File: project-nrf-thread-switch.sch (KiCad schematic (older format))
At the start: 14 parts, among them J1 Left, J2 Right

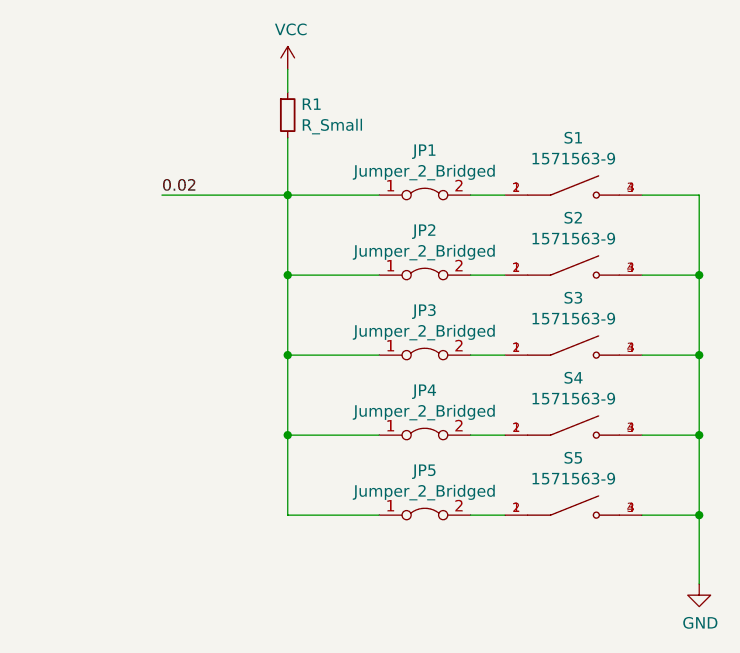
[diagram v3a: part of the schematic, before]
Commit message: Single button with header footprint fix
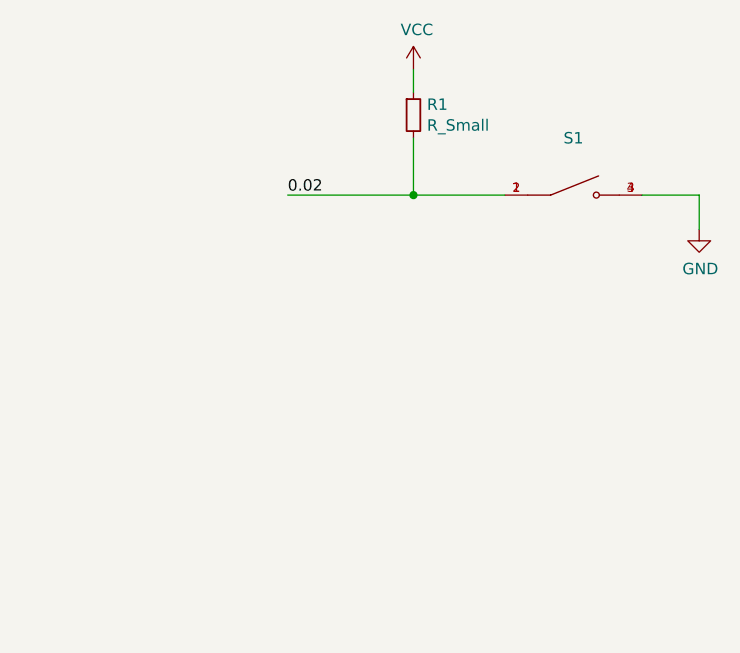
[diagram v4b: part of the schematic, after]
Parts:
- removed JP1, JP2, JP3, JP4, JP5: Jumper_2_Bridged, Jumper:SolderJumper-2_P1.3mm_Bridged_RoundedPad1.0x1.5mm, symbol Jumper:Jumper_2_Bridged
- removed S2, S3, S4, S5: 1571563-9, SW_1571563-9, symbol 1571563-9:1571563-9
- J1, J2: footprint Connector_PinSocket_2.54mm:PinSocket_1x10_P2.54mm_Vertical_SMD_Pin1Left -> Connector_PinSocket_2.54mm:PinSocket_1x10_P2.54mm_Vertical_SMD_Pin1Right
- S1: footprint SW_1571563-9 -> B3FS-1010:SW_B3FS-1010P
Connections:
- net 0.02: now also S1.1, S1.2
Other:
- moved on the sheet: R1
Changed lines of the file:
@@
 F 0 "J1" H 1728 1776 50  0000 L CNN
 F 1 "Left" H 1728 1685 50  0000 L CNN
-F 2 "Connector_PinSocket_2.54mm:PinSocket_1x10_P2.54mm_Vertical_SMD_Pin1Left" H 1700 1800 50  0001 C CNN
+F 2 "Connector_PinSocket_2.54mm:PinSocket_1x10_P2.54mm_Vertical_SMD_Pin1Right" H 1700 1800 50  0001 C CNN
 F 3 "~" H 1700 1800 50  0001 C CNN
 	1    1700 1800
@@
 F 0 "J2" H 2778 1776 50  0000 L CNN
 F 1 "Right" H 2778 1685 50  0000 L CNN
-F 2 "Connector_PinSocket_2.54mm:PinSocket_1x10_P2.54mm_Vertical_SMD_Pin1Left" H 2750 1800 50  0001 C CNN
+F 2 "Connector_PinSocket_2.54mm:PinSocket_1x10_P2.54mm_Vertical_SMD_Pin1Right" H 2750 1800 50  0001 C CNN
 F 3 "~" H 2750 1800 50  0001 C CNN
 	1    2750 1800
@@
 NoConn ~ 2350 2300
 $Comp
-L 1571563-9:1571563-9 S3
-U 1 1 6232D2C3
-P 6200 2650
-F 0 "S3" H 6200 2899 50  0000 C CNN
-F 1 "1571563-9" H 6200 2808 50  0000 C CNN
-F 2 "SW_1571563-9" H 6200 2650 50  0001 L BNN
-F 3 "" H 6200 2650 50  0001 L BNN
-F 4 "Compliant" H 6200 2650 50  0001 L BNN "EU_RoHS_Compliance"
-F 5 "1571563-9" H 6200 2650 50  0001 L BNN "Comment"
-	1    6200 2650
-	1    0    0    -1
-$EndComp
-$Comp
-L 1571563-9:1571563-9 S4
-U 1 1 62330650
-P 6200 3000
-F 0 "S4" H 6200 3249 50  0000 C CNN
-F 1 "1571563-9" H 6200 3158 50  0000 C CNN
-F 2 "SW_1571563-9" H 6200 3000 50  0001 L BNN
-F 3 "" H 6200 3000 50  0001 L BNN
-F 4 "Compliant" H 6200 3000 50  0001 L BNN "EU_RoHS_Compliance"
-F 5 "1571563-9" H 6200 3000 50  0001 L BNN "Comment"
-	1    6200 3000
-	1    0    0    -1
-$EndComp
-$Comp
-L 1571563-9:1571563-9 S5
-U 1 1 62330C79
-P 6200 3350
-F 0 "S5" H 6200 3599 50  0000 C CNN
-F 1 "1571563-9" H 6200 3508 50  0000 C CNN
-F 2 "SW_1571563-9" H 6200 3350 50  0001 L BNN
-F 3 "" H 6200 3350 50  0001 L BNN
-F 4 "Compliant" H 6200 3350 50  0001 L BNN "EU_RoHS_Compliance"
-F 5 "1571563-9" H 6200 3350 50  0001 L BNN "Comment"
-	1    6200 3350
-	1    0    0    -1
-$EndComp
-$Comp
 L BA2032SM:BA2032SM BT1
 U 1 1 623369E5
@@
 L power:GND #PWR0104
 U 1 1 6234D28E
-P 6750 3650
-F 0 "#PWR0104" H 6750 3400 50  0001 C CNN
-F 1 "GND" H 6755 3477 50  0000 C CNN
-F 2 "" H 6750 3650 50  0001 C CNN
-F 3 "" H 6750 3650 50  0001 C CNN
-	1    6750 3650
-	1    0    0    -1
-$EndComp
-Wire Wire Line
-	6500 2650 6750 2650
-Wire Wire Line
-	6750 2650 6750 3000
-Wire Wire Line
-	6750 3000 6500 3000
-Connection ~ 6750 3000
-Wire Wire Line
-	6750 3000 6750 3350
-Wire Wire Line
-	6750 3350 6500 3350
-Text Label 4400 1950 0    50   ~ 0
+P 6750 2100
+F 0 "#PWR0104" H 6750 1850 50  0001 C CNN
+F 1 "GND" H 6755 1927 50  0000 C CNN
+F 2 "" H 6750 2100 50  0001 C CNN
+F 3 "" H 6750 2100 50  0001 C CNN
+	1    6750 2100
+	1    0    0    -1
+$EndComp
+Text Label 4950 1950 0    50   ~ 0
 0.02
 $Comp
 L Device:R_Small R1
 U 1 1 62359C57
-P 4950 1600
-F 0 "R1" H 5009 1646 50  0000 L CNN
-F 1 "R_Small" H 5009 1555 50  0000 L CNN
-F 2 "Resistor_SMD:R_0603_1608Metric" H 4950 1600 50  0001 C CNN
-F 3 "~" H 4950 1600 50  0001 C CNN
-	1    4950 1600
+P 5500 1600
+F 0 "R1" H 5559 1646 50  0000 L CNN
+F 1 "R_Small" H 5559 1555 50  0000 L CNN
+F 2 "Resistor_SMD:R_0603_1608Metric" H 5500 1600 50  0001 C CNN
+F 3 "~" H 5500 1600 50  0001 C CNN
+	1    5500 1600
 	1    0    0    -1
 $EndComp
@@
 L power:VCC #PWR0105
 U 1 1 6235A371
-P 4950 1400
-F 0 "#PWR0105" H 4950 1250 50  0001 C CNN
-F 1 "VCC" H 4965 1573 50  0000 C CNN
-F 2 "" H 4950 1400 50  0001 C CNN
-F 3 "" H 4950 1400 50  0001 C CNN
-	1    4950 1400
-	1    0    0    -1
-$EndComp
-$Comp
-L Jumper:Jumper_2_Bridged JP3
-U 1 1 6235C81B
-P 5550 2650
-F 0 "JP3" H 5550 2845 50  0000 C CNN
-F 1 "Jumper_2_Bridged" H 5550 2754 50  0000 C CNN
-F 2 "Jumper:SolderJumper-2_P1.3mm_Bridged_RoundedPad1.0x1.5mm" H 5550 2650 50  0001 C CNN
-F 3 "~" H 5550 2650 50  0001 C CNN
-	1    5550 2650
-	1    0    0    -1
-$EndComp
-$Comp
-L Jumper:Jumper_2_Bridged JP4
-U 1 1 6235CF48
-P 5550 3000
-F 0 "JP4" H 5550 3195 50  0000 C CNN
-F 1 "Jumper_2_Bridged" H 5550 3104 50  0000 C CNN
-F 2 "Jumper:SolderJumper-2_P1.3mm_Bridged_RoundedPad1.0x1.5mm" H 5550 3000 50  0001 C CNN
-F 3 "~" H 5550 3000 50  0001 C CNN
-	1    5550 3000
-	1    0    0    -1
-$EndComp
-$Comp
-L Jumper:Jumper_2_Bridged JP5
-U 1 1 6235D4BC
-P 5550 3350
-F 0 "JP5" H 5550 3545 50  0000 C CNN
-F 1 "Jumper_2_Bridged" H 5550 3454 50  0000 C CNN
-F 2 "Jumper:SolderJumper-2_P1.3mm_Bridged_RoundedPad1.0x1.5mm" H 5550 3350 50  0001 C CNN
-F 3 "~" H 5550 3350 50  0001 C CNN
-	1    5550 3350
+P 5500 1400
+F 0 "#PWR0105" H 5500 1250 50  0001 C CNN
+F 1 "VCC" H 5515 1573 50  0000 C CNN
+F 2 "" H 5500 1400 50  0001 C CNN
+F 3 "" H 5500 1400 50  0001 C CNN
+	1    5500 1400
 	1    0    0    -1
 $EndComp
@@
 P 6200 1950
 F 0 "S1" H 6200 2199 50  0000 C CNN
-F 1 "1571563-9" H 6200 2108 50  0000 C CNN
-F 2 "SW_1571563-9" H 6200 1950 50  0001 L BNN
+F 1 "1571563-9" H 6200 2108 50  0001 C CNN
+F 2 "B3FS-1010:SW_B3FS-1010P" H 6200 1950 50  0001 L BNN
 F 3 "" H 6200 1950 50  0001 L BNN
 F 4 "Compliant" H 6200 1950 50  0001 L BNN "EU_RoHS_Compliance"
@@
 	1    0    0    -1
 $EndComp
-$Comp
-L 1571563-9:1571563-9 S2
-U 1 1 6236F71B
-P 6200 2300
-F 0 "S2" H 6200 2549 50  0000 C CNN
-F 1 "1571563-9" H 6200 2458 50  0000 C CNN
-F 2 "SW_1571563-9" H 6200 2300 50  0001 L BNN
-F 3 "" H 6200 2300 50  0001 L BNN
-F 4 "Compliant" H 6200 2300 50  0001 L BNN "EU_RoHS_Compliance"
-F 5 "1571563-9" H 6200 2300 50  0001 L BNN "Comment"
-	1    6200 2300
-	1    0    0    -1
-$EndComp
 Wire Wire Line
 	6500 1950 6750 1950
 Wire Wire Line
-	6750 1950 6750 2300
-Wire Wire Line
-	6750 2300 6500 2300
-$Comp
-L Jumper:Jumper_2_Bridged JP1
-U 1 1 6236F726
-P 5550 1950
-F 0 "JP1" H 5550 2145 50  0000 C CNN
-F 1 "Jumper_2_Bridged" H 5550 2054 50  0000 C CNN
-F 2 "Jumper:SolderJumper-2_P1.3mm_Bridged_RoundedPad1.0x1.5mm" H 5550 1950 50  0001 C CNN
-F 3 "~" H 5550 1950 50  0001 C CNN
-	1    5550 1950
-	1    0    0    -1
-$EndComp
-$Comp
-L Jumper:Jumper_2_Bridged JP2
-U 1 1 6236F72C
-P 5550 2300
-F 0 "JP2" H 5550 2495 50  0000 C CNN
-F 1 "Jumper_2_Bridged" H 5550 2404 50  0000 C CNN
-F 2 "Jumper:SolderJumper-2_P1.3mm_Bridged_RoundedPad1.0x1.5mm" H 5550 2300 50  0001 C CNN
-F 3 "~" H 5550 2300 50  0001 C CNN
-	1    5550 2300
-	1    0    0    -1
-$EndComp
-Wire Wire Line
-	6750 2300 6750 2650
-Connection ~ 6750 2300
-Connection ~ 6750 2650
-Wire Wire Line
-	5750 1950 5900 1950
-Wire Wire Line
-	5900 2300 5750 2300
-Wire Wire Line
-	5750 2650 5900 2650
-Wire Wire Line
-	5750 3000 5900 3000
-Wire Wire Line
-	5900 3350 5750 3350
-Wire Wire Line
-	4950 1400 4950 1500
-Wire Wire Line
-	4400 1950 4950 1950
-Wire Wire Line
-	4950 1700 4950 1950
-Connection ~ 4950 1950
-Wire Wire Line
-	4950 1950 5350 1950
-Wire Wire Line
-	5350 2300 4950 2300
-Wire Wire Line
-	4950 2300 4950 1950
-Wire Wire Line
-	4950 2300 4950 2650
-Connection ~ 4950 2300
-Wire Wire Line
-	5350 2650 4950 2650
-Connection ~ 4950 2650
-Wire Wire Line
-	4950 2650 4950 3000
-Wire Wire Line
-	5350 3000 4950 3000
-Connection ~ 4950 3000
-Wire Wire Line
-	4950 3000 4950 3350
-Wire Wire Line
-	5350 3350 4950 3350
-Wire Wire Line
-	6750 3650 6750 3350
-Connection ~ 6750 3350
+	5500 1400 5500 1500
+Wire Wire Line
+	4950 1950 5500 1950
+Wire Wire Line
+	5500 1700 5500 1950
+Connection ~ 5500 1950
+Wire Wire Line
+	5500 1950 5900 1950
+Wire Wire Line
+	6750 1950 6750 2100
 $EndSCHEMATC
